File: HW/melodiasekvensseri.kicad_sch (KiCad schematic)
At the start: 30 parts, among them J2 Clock_In, J3 Gate_Out, J4 CV_Out, J5 Conn_02x03_Odd_Even, J6 Conn_01x04, U1 TLV2372IP

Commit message: Pin remapping, connect AVCC, filtering, TP
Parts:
- added C14: 100n, Capacitor_THT:C_Disc_D5.0mm_W2.5mm_P5.00mm, symbol Device:C
- added R8: 10, Resistor_THT:R_Axial_DIN0207_L6.3mm_D2.5mm_P10.16mm_Horizontal, symbol Device:R
- added TP_A5V1, TP_D5V1, TP_DAC_OUT1: TestPoint, TestPoint:TestPoint_Pad_2.0x2.0mm, symbol Connector:TestPoint
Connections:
- net BUTTON_IN is gone; now on net ENC_B: MC1.26 (PC3)
- net A_+5V: now also TP_A5V1.1
- net CLK_IN: now also MC1.5 (PD3); no longer MC1.14 (PB0)
- net DEMUX_A: now also MC1.12 (PD6); no longer MC1.13 (PD7)
- net DEMUX_B: now also MC1.13 (PD7); no longer MC1.12 (PD6)
- net DEMUX_C: now also MC1.14 (PB0); no longer MC1.11 (PD5)
- net D_+5V: now also R8.1, TP_D5V1.1
- net D_GND: now also C14.1
- net ENC_A: now also MC1.4 (PD2); no longer MC1.5 (PD3)
- net ENC_B: no longer MC1.4 (PD2)
- net RXD: now also J6.1 (Pin_1); no longer J6.2 (Pin_2)
- net TXD: now also J6.2 (Pin_2); no longer J6.1 (Pin_1)
- net at DAC1.8 (VOUT), U1.3 (1IN+): now also TP_DAC_OUT1.1
- net at MC1.20 (AVCC): now also C14.2, R8.2
- new net STEP_IN: MC1.11 (PD5)
- no-connect marks 12 -> 11

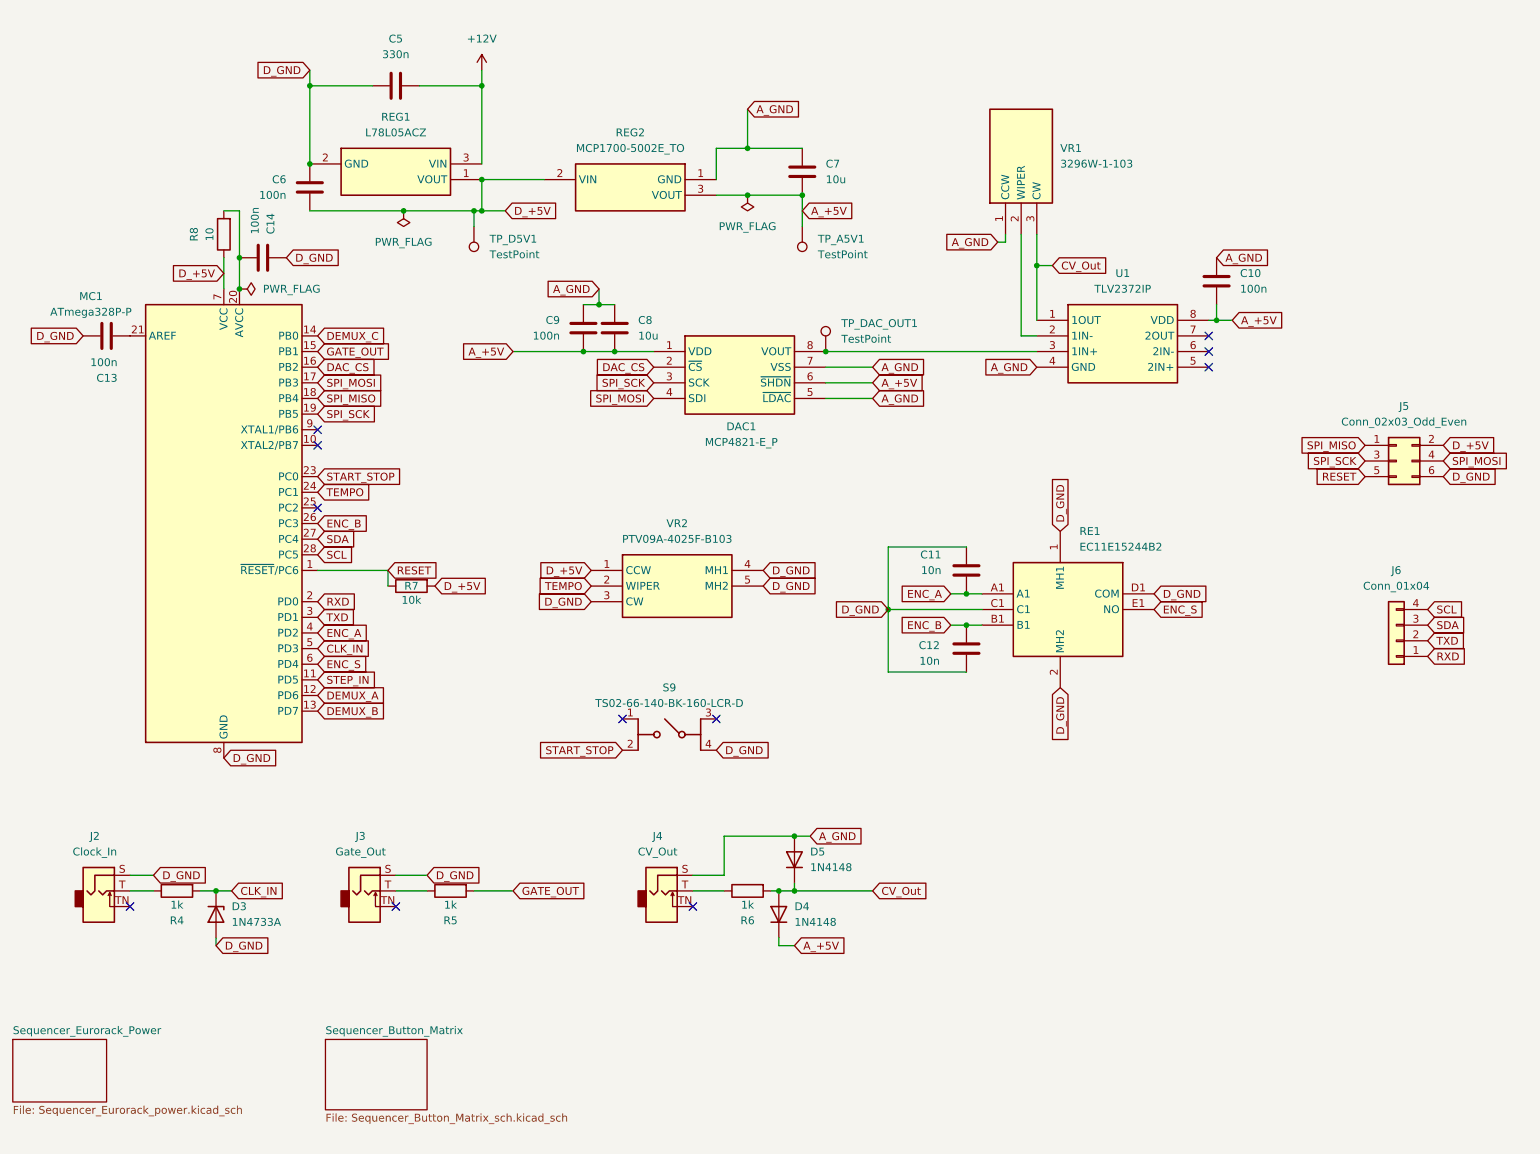
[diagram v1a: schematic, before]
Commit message: Panel clearances, switched REG1, added test code
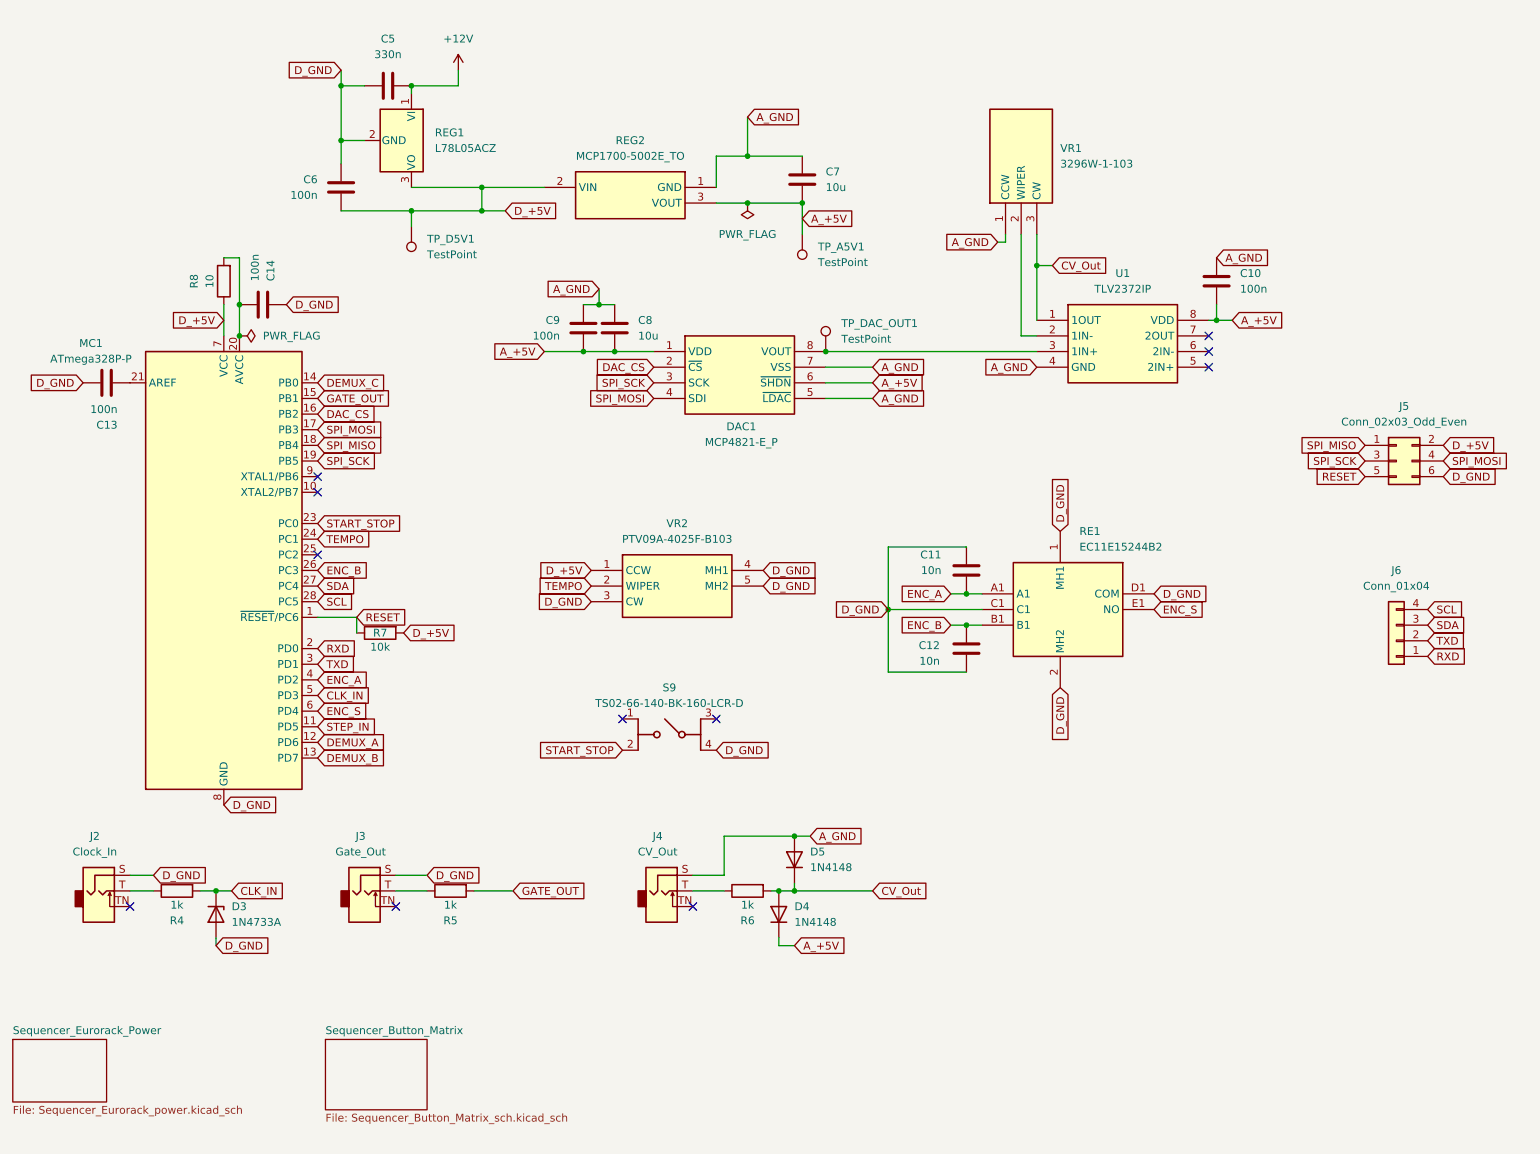
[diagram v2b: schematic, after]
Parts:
- REG1: footprint Project_Libraries:L78L05ACZ -> Package_TO_SOT_THT:TO-220-3_Vertical; symbol L78L05ACZ:L78L05ACZ -> Regulator_Linear:LM78M05_TO220
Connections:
- net +12V: now also REG1.1 (VI); no longer REG1.3 (VIN)
- net D_+5V: now also REG1.3 (VO); no longer REG1.1 (VOUT)
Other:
- moved on the sheet: C13, C14, C5, C6, C7, MC1, R7, R8, REG1, REG2, TP_A5V1, TP_D5V1

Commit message: Updated REG1 model name
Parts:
- REG1: value L78L05ACZ -> LM78M05
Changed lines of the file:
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@@
 			)
 		)
-		(property "Value" "L78L05ACZ"
+		(property "Value" "LM78M05"
 			(at 86.36 34.2899 90)
 			(show_name no)

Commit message: Removed CV_OUT diodes, filtering cap added
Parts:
- removed D4, D5: 1N4148, Diode_THT:D_DO-35_SOD27_P7.62mm_Horizontal, symbol Diode:1N4148
- added C15: 100n, Capacitor_THT:C_Disc_D5.0mm_W2.5mm_P5.00mm, symbol Device:C
- TP_CV_OUT1: renamed from TP_DAC_OUT1; footprint TestPoint:TestPoint_Pad_2.0x2.0mm -> TestPoint:TestPoint_THTPad_2.0x2.0mm_Drill1.0mm
- renumbered D3 to D2
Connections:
- net CV_Out: now also TP_CV_OUT1.1
- net D_+5V: now also C15.2
- net D_GND: now also C15.1
- net at DAC1.8 (VOUT), U1.3 (1IN+): no longer TP_CV_OUT1.1
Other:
- moved on the sheet: TP_CV_OUT1

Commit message: Some resistor footprints changed
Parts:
- R4, R5, R6: footprint Resistor_THT:R_Axial_DIN0207_L6.3mm_D2.5mm_P10.16mm_Horizontal -> Resistors_Universal.pretty-master:Resistor_SMD+THTuniversal_0805to1206_RM10_HandSoldering_RevA_Date25Jun2010
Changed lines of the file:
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@@
 			)
 		)
-		(property "Footprint" "Resistor_THT:R_Axial_DIN0207_L6.3mm_D2.5mm_P10.16mm_Horizontal"
+		(property "Footprint" "Resistors_Universal.pretty-master:Resistor_SMD+THTuniversal_0805to1206_RM10_HandSoldering_RevA_Date25Jun2010"
 			(at 88.9 153.162 90)
 			(hide yes)
@@
 			)
 		)
-		(property "Footprint" "Resistor_THT:R_Axial_DIN0207_L6.3mm_D2.5mm_P10.16mm_Horizontal"
+		(property "Footprint" "Resistors_Universal.pretty-master:Resistor_SMD+THTuniversal_0805to1206_RM10_HandSoldering_RevA_Date25Jun2010"
 			(at 44.45 153.162 90)
 			(hide yes)
@@
 			)
 		)
-		(property "Footprint" "Resistor_THT:R_Axial_DIN0207_L6.3mm_D2.5mm_P10.16mm_Horizontal"
+		(property "Footprint" "Resistors_Universal.pretty-master:Resistor_SMD+THTuniversal_0805to1206_RM10_HandSoldering_RevA_Date25Jun2010"
 			(at 137.16 153.162 90)
 			(hide yes)

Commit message: REG2 changed, grounding fixes, routing changes
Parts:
- removed C7: 10u, Capacitor_THT:C_Disc_D5.0mm_W2.5mm_P5.00mm, symbol Device:C
- removed REG2: MCP1700-5002E_TO, Project_Libraries:TO127P254X495-3, symbol MCP1700-5002E_TO:MCP1700-5002E_TO
- added C16: 100n, Capacitor_THT:C_Disc_D5.0mm_W2.5mm_P5.00mm, symbol Device:C
- added C17: 330n, Capacitor_THT:C_Disc_D5.0mm_W2.5mm_P5.00mm, symbol Device:C
- added H1, H2, H3, H4: MountingHole, MountingHole:MountingHole_3.2mm_M3, symbol Mechanical:MountingHole
- added REG2: L78L05ACZ, Project_Libraries:L78L05ACZ, symbol L78L05ACZ:L78L05ACZ
- TP_CV_OUT1: footprint TestPoint:TestPoint_THTPad_2.0x2.0mm_Drill1.0mm -> TestPoint:TestPoint_THTPad_1.5x1.5mm_Drill0.7mm
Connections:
- net +12V: now also C17.2, REG2.3 (VIN)
- net A_+5V: now also C16.2, REG2.1 (VOUT)
- net A_GND: now also C16.1, C17.1, REG2.2 (GND)
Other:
- moved on the sheet: TP_A5V1

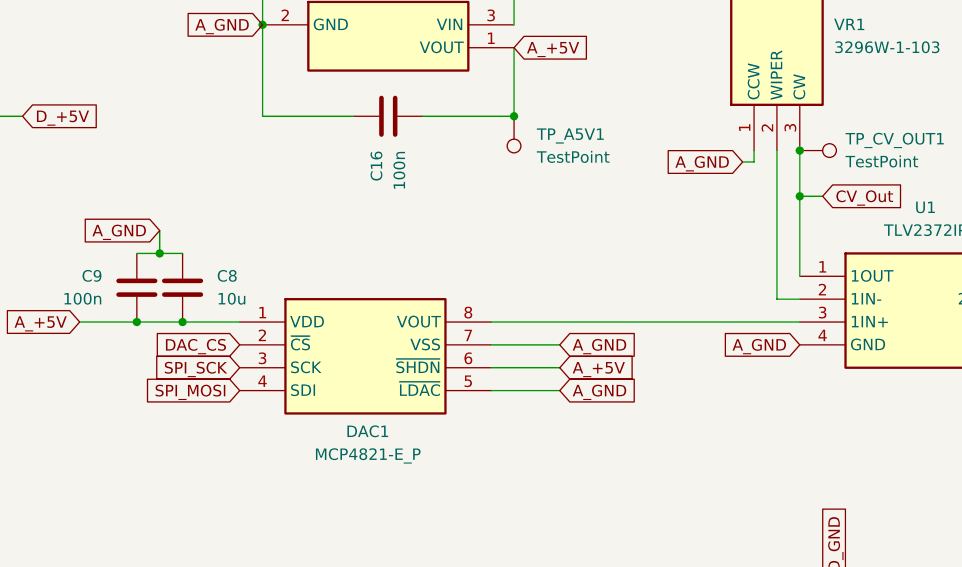
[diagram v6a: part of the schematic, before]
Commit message: Moved or added decoupling caps, moved test points
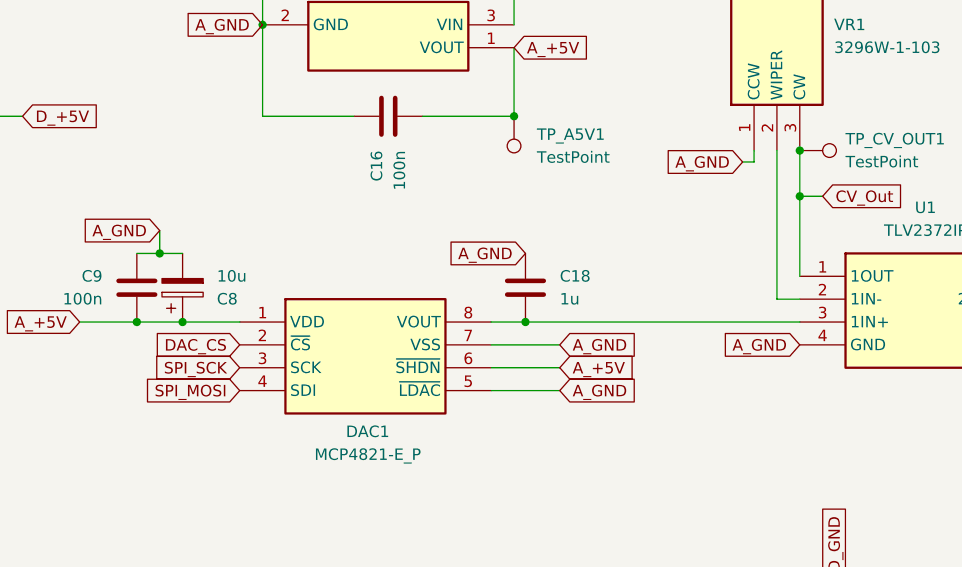
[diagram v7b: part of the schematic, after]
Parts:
- added C18: 1u, Capacitor_THT:C_Disc_D5.0mm_W2.5mm_P5.00mm, symbol Device:C
- C8: symbol Device:C -> Device:C_Polarized
- TP_A5V1, TP_D5V1: footprint TestPoint:TestPoint_Pad_2.0x2.0mm -> TestPoint:TestPoint_THTPad_1.5x1.5mm_Drill0.7mm
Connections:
- net A_+5V: now also C8.1; no longer C8.2
- net A_GND: now also C8.2, C18.1; no longer C8.1
- net at DAC1.8 (VOUT), U1.3 (1IN+): now also C18.2
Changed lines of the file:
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@@
 	)
 	(junction
+		(at 115.57 67.31)
+		(diameter 0)
+		(color 0 0 0 0)
+	)
+	(junction
 		(at 172.72 111.76)
 		(diameter 0)
@@
 	)
 	(junction
-		(at 115.57 67.31)
+		(at 153.67 67.31)
 		(diameter 0)
 		(color 0 0 0 0)
@@
 	(wire
 		(pts
-			(xy 149.86 67.31) (xy 184.15 67.31)
+			(xy 149.86 67.31) (xy 153.67 67.31)
 		)
 		(stroke
@@
 	(wire
 		(pts
+			(xy 115.57 67.31) (xy 121.92 67.31)
+		)
+		(stroke
+			(width 0)
+			(type default)
+		)
+	)
+	(wire
+		(pts
 			(xy 149.86 74.93) (xy 157.48 74.93)
 		)
@@
 	(wire
 		(pts
-			(xy 134.62 44.45) (xy 124.46 44.45)
+			(xy 153.67 67.31) (xy 184.15 67.31)
 		)
 		(stroke
@@
 	(wire
 		(pts
-			(xy 71.12 33.02) (xy 74.93 33.02)
+			(xy 134.62 44.45) (xy 124.46 44.45)
 		)
 		(stroke
@@
 	(wire
 		(pts
-			(xy 73.66 110.49) (xy 73.66 113.03)
+			(xy 71.12 33.02) (xy 74.93 33.02)
 		)
 		(stroke
@@
 	(wire
 		(pts
-			(xy 152.4 36.83) (xy 152.4 44.45)
+			(xy 73.66 110.49) (xy 73.66 113.03)
 		)
 		(stroke
@@
 	(wire
 		(pts
-			(xy 115.57 67.31) (xy 121.92 67.31)
+			(xy 152.4 36.83) (xy 152.4 44.45)
 		)
 		(stroke
@@
 	(global_label "A_GND"
 		(shape input)
+		(at 153.67 59.69 180)
+		(fields_autoplaced yes)
+		(effects
+			(font
+				(size 1.27 1.27)
+			)
+			(justify right)
+		)
+		(property "Intersheetrefs" "${INTERSHEET_REFS}"
+			(at 144.7581 59.69 0)
+			(hide yes)
+			(show_name no)
+			(do_not_autoplace no)
+			(effects
+				(font
+					(size 1.27 1.27)
+				)
+				(justify right)
+			)
+		)
+	)
+	(global_label "A_GND"
+		(shape input)
 		(at 113.03 57.15 180)
 		(fields_autoplaced yes)
@@
 			)
 		)
-		(property "Footprint" "TestPoint:TestPoint_Pad_2.0x2.0mm"
+		(property "Footprint" "TestPoint:TestPoint_THTPad_1.5x1.5mm_Drill0.7mm"
 			(at 147.32 44.45 0)
 			(hide yes)
@@
 	)
 	(symbol
-		(lib_id "Device:C")
+		(lib_id "Device:C_Polarized")
 		(at 115.57 63.5 0)
+		(mirror x)
 		(unit 1)
 		(body_style 1)
@@
 		(dnp no)
 		(property "Reference" "C8"
-			(at 119.38 62.2299 0)
+			(at 119.38 64.7701 0)
 			(show_name no)
 			(do_not_autoplace no)
@@
 		)
 		(property "Value" "10u"
-			(at 119.38 64.7699 0)
+			(at 119.38 62.2301 0)
 			(show_name no)
 			(do_not_autoplace no)
@@
 		)
 		(property "Footprint" "Capacitor_THT:C_Disc_D5.0mm_W2.5mm_P5.00mm"
-			(at 116.5352 67.31 0)
+			(at 116.5352 59.69 0)
 			(hide yes)
 			(show_name no)
@@
 			)
 		)
-		(property "Description" "Unpolarized capacitor"
+		(property "Description" "Polarized capacitor"
 			(at 115.57 63.5 0)
 			(hide yes)
@@
 			)
 		)
-		(property "Footprint" "TestPoint:TestPoint_Pad_2.0x2.0mm"
+		(property "Footprint" "TestPoint:TestPoint_THTPad_1.5x1.5mm_Drill0.7mm"
 			(at 77.47 46.99 0)
 			(hide yes)
@@
 					(unit 1)
 				)
+			)
+		)
+	)
+	(symbol
+		(lib_id "Device:C")
+		(at 153.67 63.5 0)
+		(unit 1)
+		(body_style 1)
+		(exclude_from_sim no)
+		(in_bom yes)
+		(on_board yes)
+		(in_pos_files yes)
+		(dnp no)
+		(property "Reference" "C18"
+			(at 157.48 62.2299 0)
+			(show_name no)
+			(do_not_autoplace no)
+			(effects
+				(font
+					(size 1.27 1.27)
+				)
+				(justify left)
+			)
+		)
+		(property "Value" "1u"
+			(at 157.48 64.7699 0)
+			(show_name no)
+			(do_not_autoplace no)
+			(effects
+				(font
+					(size 1.27 1.27)
+				)
+				(justify left)
+			)
+		)
+		(property "Footprint" "Capacitor_THT:C_Disc_D5.0mm_W2.5mm_P5.00mm"
+			(at 154.6352 67.31 0)
+			(hide yes)
+			(show_name no)
+			(do_not_autoplace no)
+			(effects
+				(font
+					(size 1.27 1.27)
+				)
+			)
+		)
+		(property "Datasheet" ""
+			(at 153.67 63.5 0)
+			(hide yes)
+			(show_name no)
+			(do_not_autoplace no)
+			(effects
+				(font
+					(size 1.27 1.27)
+				)
+			)
+		)
+		(property "Description" "Unpolarized capacitor"
+			(at 153.67 63.5 0)
+			(hide yes)
+			(show_name no)
+			(do_not_autoplace no)
+			(effects
+				(font
+					(size 1.27 1.27)
+				)
+			)
+		)
+		(pin "2"
+		)
+		(pin "1"
+		)
+		(instances
+			(project "melodiasekvensseri"
+				(path "/88d7c3ef-0a1d-4476-9115-c0d0977d43dc"
+					(reference "C18")
+					(unit 1)
+				)
